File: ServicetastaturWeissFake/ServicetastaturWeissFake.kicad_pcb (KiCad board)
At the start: 2 copper layers, 153.7 x 57.2 mm, 67 parts, among them J1 Automat, SW1 Gewinn, SW10 Lautspr./, SW11 ↓0,10, SW12 ↑0,10, SW13 ↓Serie, SW14 ↑Serie, SW15 Zeit, SW16 ↑1,-, SW17 ↙0,10, SW18 ↙1,-, SW19 Auszahlquote, SW2 Foul, SW20 ↙5,-, SW21 Münzsp., SW22 Sp.Zähl, SW23 Lampen, SW24 Reset, SW25 Initialisieren, SW26 Münzung, SW27 Ende, SW28 ↑0,10, SW29 ↓Serie, SW3 ↙2,-, SW30 ↑Serie, SW31 ↓1,-, SW32 ↑1,-, SW4 HW-Test, SW5 Münzsp., SW6 Sp.Zähl, SW7 Dauerlauf, SW8 Reset, SW9 Initialisieren, U1 CC56-12CGKWA, U2 CC56-12CGKWA, U3 74LS48, U4 74LS145

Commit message: schieberei
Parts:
- added REF**: KiCad-Logo2_6mm_SilkScreen, Symbol:KiCad-Logo2_6mm_SilkScreen, B.Cu at (55.2, 35.6)
- added REF**: Symbol_CC-ShareAlike_CopperTop_Big, Symbol:Symbol_CC-ShareAlike_CopperTop_Big, B.Cu at (88.9, 38.1)
- moved REF** 3.64 mm to (32.4, 36.2)
- moved REF** 2.81 mm to (41.9, 36.8)
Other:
- board text added: "JLCJLCJLCJLC"
- board text added: "Materialwert unter 10€"
- board text added: "Produktionsdaten gibt es gratis online,"
- board text removed: "Wenn du mehr als 15€ bezahlt hast, wurdest du über den Tisch gezogen."

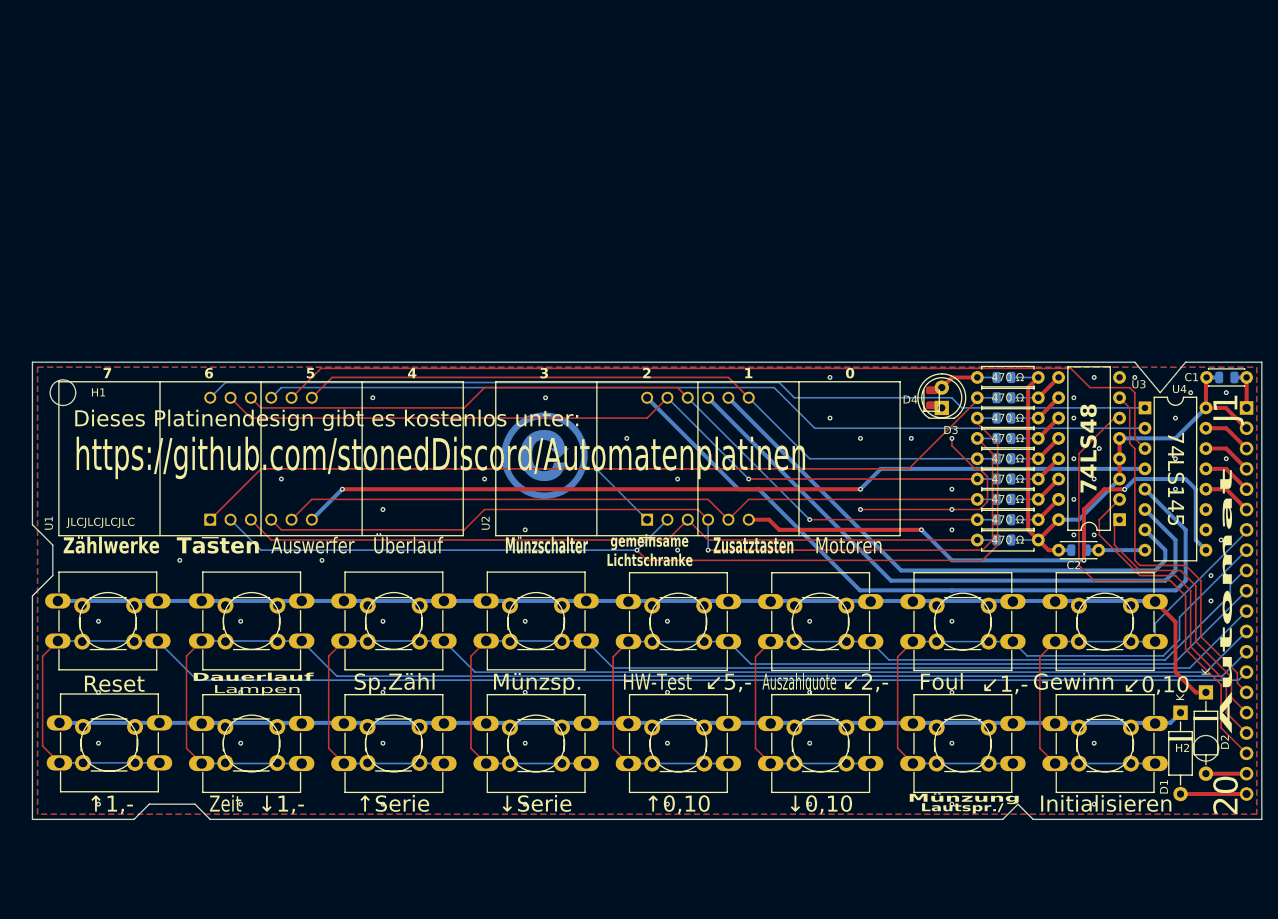
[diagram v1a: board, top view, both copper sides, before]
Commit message: b3f schalter und displays gedreht
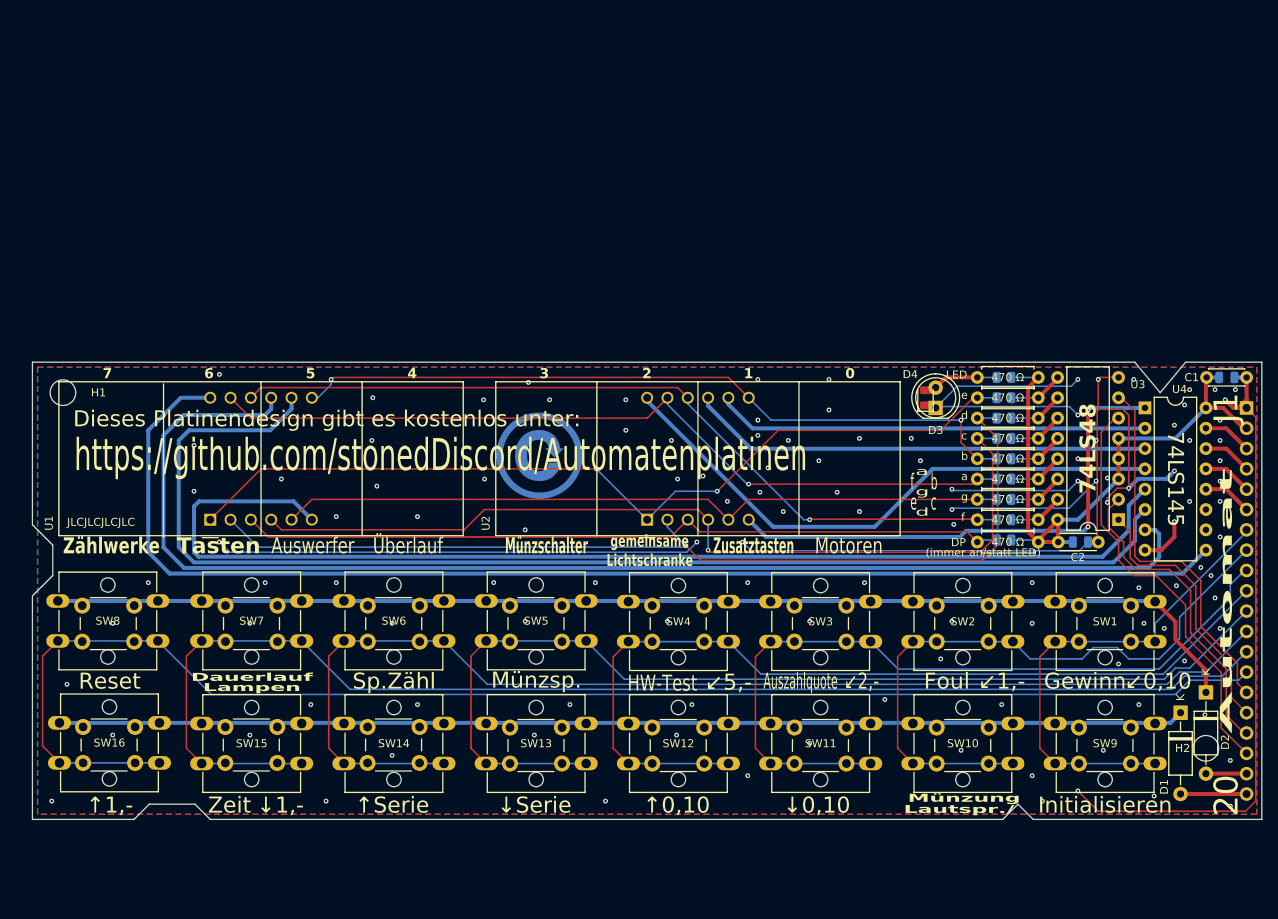
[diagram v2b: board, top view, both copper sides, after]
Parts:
- SW1, SW10, SW11, SW12, SW13, SW14, SW15, SW16, SW2, SW3, SW4, SW5, SW6, SW7, SW8, SW9: footprint Button_Switch_THT:SW_PUSH-12mm -> Button_Switch_THT:SW_SPST_Omron_B3F-40xx
- moved C4 1.03 mm to (155.9, 48.9)
- moved C2 1.02 mm to (153.1, 48.9)
- moved D3 0.76 mm to (137.8, 32.1)
- moved D4 0.76 mm to (136.5, 30.9)
- moved REF** 0.64 mm to (88.3, 38.1)
- moved R8 0.25 mm to (150.6, 48.9)
- moved U3 0.13 mm to (160.7, 46.1)
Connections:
- U4 pad 1: Net-(U1-CC1) -> Net-(U2-CC4)
- U4 pad 2: Net-(U1-CC2) -> Net-(U2-CC3)
- U4 pad 3: Net-(U1-CC3) -> Net-(U2-CC2)
- U4 pad 4: Net-(U1-CC4) -> Net-(U2-CC1)
- U4 pad 5: Net-(U2-CC1) -> Net-(U1-CC4)
- U4 pad 6: Net-(U2-CC2) -> Net-(U1-CC3)
- U4 pad 7: Net-(U2-CC3) -> Net-(U1-CC2)
- U4 pad 9: Net-(U2-CC4) -> Net-(U1-CC1)
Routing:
- net GND: track 39.3 -> 314.2 mm, vias 69 -> 123
- net Net-(U1-CC2): track 111.9 -> 161.2 mm
- net Net-(U1-CC3): track 115.7 -> 156.3 mm
- net Net-(U1-CC1): track 118.9 -> 159.2 mm
- net Net-(U1-CC4): track 106.8 -> 146.1 mm, vias 2 -> 0
- net Net-(U2-CC2): track 77.6 -> 57.9 mm
- net Net-(U2-CC1): track 91.4 -> 72.1 mm
- net Net-(U2-CC3): track 68.9 -> 54.1 mm
- net Net-(U2-CC4): track 74.6 -> 65.7 mm, vias 3 -> 2
- net /A3: track 58.6 -> 52.7 mm
- net Net-(U1-e): track 113.8 -> 109.9 mm, vias 1 -> 2
- net +5V: track 75.1 -> 78.3 mm
- net Net-(U1-b): track 90.9 -> 92.9 mm, vias 0 -> 2
- net /TS7: track 180.4 -> 181.9 mm
- net /TS1: track 78.9 -> 80.3 mm
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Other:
- board text added: "(immer an/statt LED)"
- board text added: "DP"
- board text added: "Die Produkt ionsdaten gibt es gratis online,"
- board text added: "LED"
- board text added: "Spalten"
- board text added: "Wird die Taste {dblquote}HW⁻Test{dblquote} bzw. die Taste {dblquote}Serienspiele{dblquote} betätigt und das Gerät ist mit dieser Sicherung ausgestattet, erscheinen im Testgeräte-Display drei zufällig ausgewählte Ziffern aus dem hexadezimalen Zahlencode."
- board text added: "Zeichen"
- board text added: "a"
- board text added: "b"
- board text added: "c"
- board text added: "d"
- board text added: "e"
- board text added: "f"
- board text added: "g"
- board text removed: "Produktionsdaten gibt es gratis online,"
- board text removed: "Wird die Taste {dblquote}HW⁻Test{dblquote} bzw. die Taste {dblquote}Serienspiele{dblquote} betätigt und das Gerät ist mit dieser Sicherung ausgestattet, erscheinen im Testgeräte-Displaz drei zufällig ausgewählte Ziffern aus dem hexadezimalen Zahlencode."
- board text removed: "ざわ・・・"

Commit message: doppelIC
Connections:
- U3 pad 4: +5V -> Net-(JP1-C)
- U4 pad 10: unconnected-(U4-Q8-Pad10) -> Net-(JP1-A)
- U4 pad 11: unconnected-(U4-Q9-Pad11) -> Net-(JP1-A)
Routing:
- net +5V: track 78.3 -> 103.6 mm
- net GND: vias 123 -> 122
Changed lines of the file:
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@@
 	(net 45 "Net-(U2-CC4)")
 	(net 46 "Net-(U2-CC1)")
-	(net 47 "unconnected-(U4-Q8-Pad10)")
-	(net 48 "unconnected-(U4-Q9-Pad11)")
+	(net 47 "Net-(JP1-C)")
+	(net 48 "Net-(JP1-A)")
 	(footprint "Button_Switch_THT:SW_PUSH_6mm"
 		(layer "F.Cu")
@@
 			(layers "*.Cu" "*.Mask")
 			(remove_unused_layers no)
-			(net 9 "+5V")
+			(net 47 "Net-(JP1-C)")
 			(pinfunction "BI")
 			(pintype "input")
@@
 			(layers "*.Cu" "*.Mask")
 			(remove_unused_layers no)
-			(net 47 "unconnected-(U4-Q8-Pad10)")
+			(net 48 "Net-(JP1-A)")
 			(pinfunction "Q8")
-			(pintype "open_collector+no_connect")
+			(pintype "open_collector")
 		)
 		(pad "11" thru_hole oval
@@
 			(layers "*.Cu" "*.Mask")
 			(remove_unused_layers no)
-			(net 48 "unconnected-(U4-Q9-Pad11)")
+			(net 48 "Net-(JP1-A)")
 			(pinfunction "Q9")
-			(pintype "open_collector+no_connect")
+			(pintype "open_collector")
 		)
 		(pad "12" thru_hole oval
@@
 		(tags "capacitor")
 		(property "Reference" "C4"
-			(at 0 1.68 360)
+			(at 0 1.68 0)
 			(layer "B.SilkS")
 			(effects
@@
 		)
 		(property "Value" "C"
-			(at 0 -1.68 360)
+			(at 0 -1.68 0)
 			(layer "B.Fab")
 			(effects
@@
 		)
 		(fp_text user "${REFERENCE}"
-			(at 0 0 360)
+			(at 0 0 0)
 			(layer "B.Fab")
 			(effects
@@
 	)
 	(segment
-		(start 150.622 48.641)
-		(end 153.035 46.228)
+		(start 150.622 28.321)
+		(end 151.927 27.016)
+		(width 0.2)
+		(layer "F.Cu")
+		(net 9)
+	)
+	(segment
+		(start 159.385 37.211)
+		(end 159.385 39.751)
 		(width 0.5)
 		(layer "F.Cu")
@@
 	)
 	(segment
-		(start 160.655 41.021)
-		(end 160.655 35.941)
+		(start 150.622 48.641)
+		(end 153.035 46.228)
 		(width 0.5)
 		(layer "F.Cu")
@@
 	)
 	(segment
+		(start 165.605173 30.846037)
+		(end 166.118827 30.846037)
+		(width 0.2)
+		(layer "F.Cu")
+		(net 9)
+	)
+	(segment
 		(start 153.115 48.895)
 		(end 150.622 48.895)
@@
 	)
 	(segment
+		(start 159.385 39.751)
+		(end 160.655 41.021)
+		(width 0.5)
+		(layer "F.Cu")
+		(net 9)
+	)
+	(segment
+		(start 166.118827 30.846037)
+		(end 168.643864 28.321)
+		(width 0.2)
+		(layer "F.Cu")
+		(net 9)
+	)
+	(segment
+		(start 160.655 35.941)
+		(end 159.385 37.211)
+		(width 0.5)
+		(layer "F.Cu")
+		(net 9)
+	)
+	(segment
+		(start 168.643864 28.321)
+		(end 171.657 28.321)
+		(width 0.2)
+		(layer "F.Cu")
+		(net 9)
+	)
+	(segment
 		(start 153.035 46.228)
 		(end 153.035 46.101)
@@
 	)
 	(segment
+		(start 151.927 27.016)
+		(end 161.775136 27.016)
+		(width 0.2)
+		(layer "F.Cu")
+		(net 9)
+	)
+	(segment
+		(start 161.775136 27.016)
+		(end 165.605173 30.846037)
+		(width 0.2)
+		(layer "F.Cu")
+		(net 9)
+	)
+	(segment
 		(start 149.352 29.591)
 		(end 149.352 47.625)
@@
 	)
 	(via
-		(at 159.258 40.894)
-		(size 0.6)
-		(drill 0.3)
-		(layers "F.Cu" "B.Cu")
-		(free yes)
-		(net 16)
-	)
-	(via
 		(at 96.52 81.28)
 		(size 0.6)
@@
 	)
 	(via
-		(at 162.56 28.575)
+		(at 162.4963 28.605978)
 		(size 0.6)
 		(drill 0.3)

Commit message: kleine LED
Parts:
- added JP1: Jumper_3_Bridged12, Jumper:SolderJumper-3_P1.3mm_Bridged12_Pad1.0x1.5mm_NumberLabels, B.Cu at (161.0, 31.8)
- added U5: 74LS48, Package_SO:SOIC-16_4.55x10.3mm_P1.27mm, F.Cu at (151.2, 38.1)
- added U6: 74LS145, Package_SO:SOIC-16_4.55x10.3mm_P1.27mm, F.Cu at (165.2, 41.3)
- C3, C4, R10, R11, R12, R13, R14, R15, R16, R17, R18: moved to F.Cu
- D3: footprint LED_THT:LED_D5.0mm -> LED_THT:LED_D3.0mm
- moved C4 9.34 mm to (146.6, 48.5), turned to 180 degrees
- moved C2 6.53 mm to (150.1, 54.7), turned to -90 degrees
- moved R6 5.57 mm to (145.7, 43.6)
- moved R7 5.35 mm to (145.7, 41.5)
- moved R1 5.18 mm to (145.7, 39.5)
- moved R15 5.12 mm to (141.9, 43.6)
- moved R2 5.06 mm to (145.7, 37.5)
- moved R3 4.98 mm to (145.7, 35.4)
- moved R4 4.95 mm to (145.7, 33.4)
- moved R16 4.89 mm to (141.9, 41.5)
- moved R10 4.70 mm to (141.9, 39.5)
- moved R11 4.56 mm to (141.9, 37.5)
- moved R12 4.47 mm to (141.9, 35.4)
- moved R13 4.44 mm to (141.9, 33.4)
- moved R8 3.68 mm to (148.1, 46.2)
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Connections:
- R17 pad 2: Net-(U1-DPX) -> unconnected-(R17-Pad2)
- R8 pad 2: Net-(U1-DPX) -> unconnected-(R17-Pad2)
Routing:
- net GND: track 314.2 -> 111.9 mm, vias 122 -> 85
- net Net-(U1-DPX): track 96.3 -> 56.4 mm
- net Net-(JP1-A): track 0.00 -> 30.7 mm, vias 0 -> 1
- net Net-(U2-CC3): track 54.1 -> 79.2 mm
- net Net-(U2-CC2): track 57.9 -> 78.7 mm
- net Net-(U1-d): track 122.5 -> 103.6 mm
- net Net-(U1-c): track 112.7 -> 95.1 mm, vias 1 -> 2
- net Net-(JP1-C): track 0.00 -> 11.8 mm
- net /A1: track 33.5 -> 42.8 mm, vias 0 -> 2
- net /A3: track 52.7 -> 61.9 mm
- net Net-(U2-CC1): track 72.1 -> 80.7 mm
- net /A0: track 46.7 -> 54.9 mm
- net Net-(U1-e): track 109.9 -> 117.5 mm, vias 2 -> 1
- net Net-(U1-b): track 92.9 -> 86.4 mm, vias 2 -> 1
- net Net-(U1-CC1): track 159.2 -> 165.7 mm
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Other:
- outline, holes or cut-outs redrawn
- board text removed: "(immer an/statt LED)"
- board text removed: "DP"
- board text removed: "LED"
- board text removed: "Spalten"
- board text removed: "Zeichen"
- board text removed: "a"
- board text removed: "b"
- board text removed: "c"
- board text removed: "d"
- board text removed: "e"
- board text removed: "f"
- board text removed: "g"

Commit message: rumgeschiebe
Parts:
- moved SW8 0.20 mm to (28.3, 56.3)
- moved SW16 0.08 mm to (28.3, 71.6)

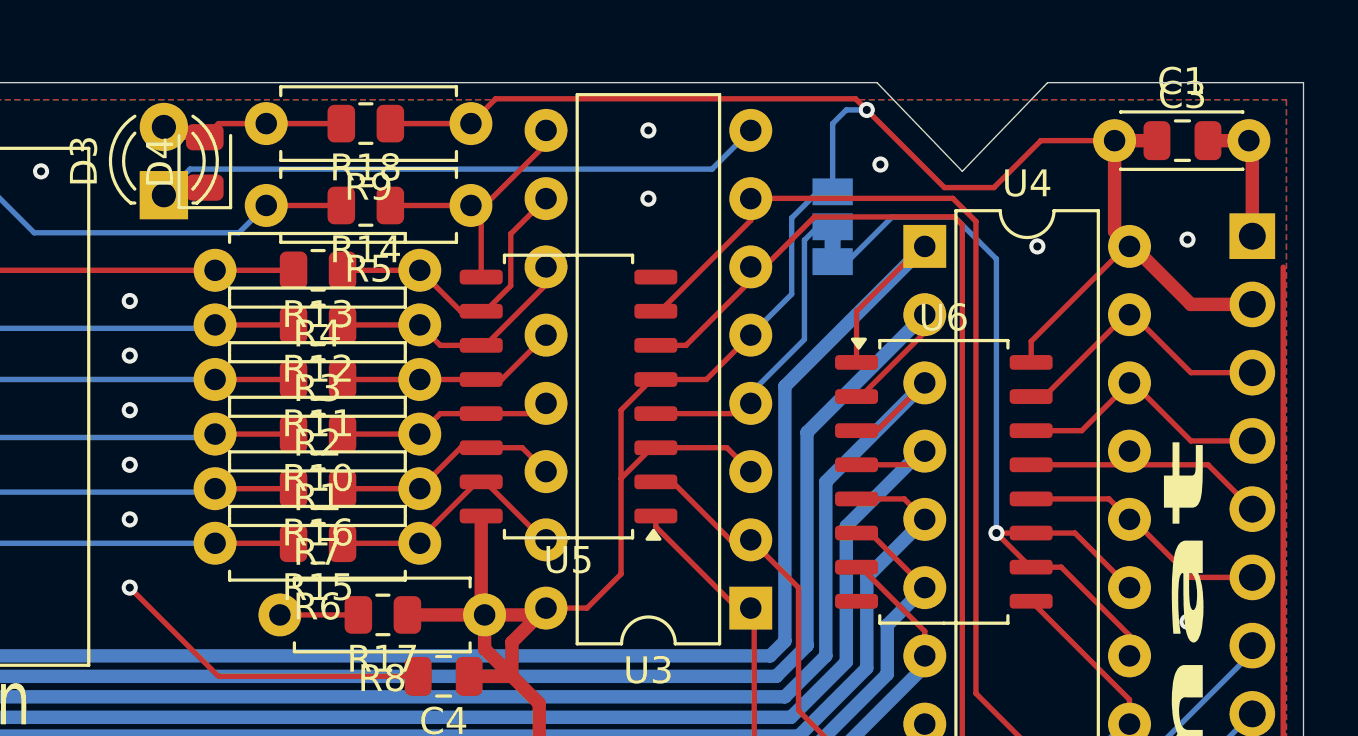
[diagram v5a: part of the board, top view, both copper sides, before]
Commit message: Update ServicetastaturWeissFake.kicad_pcb
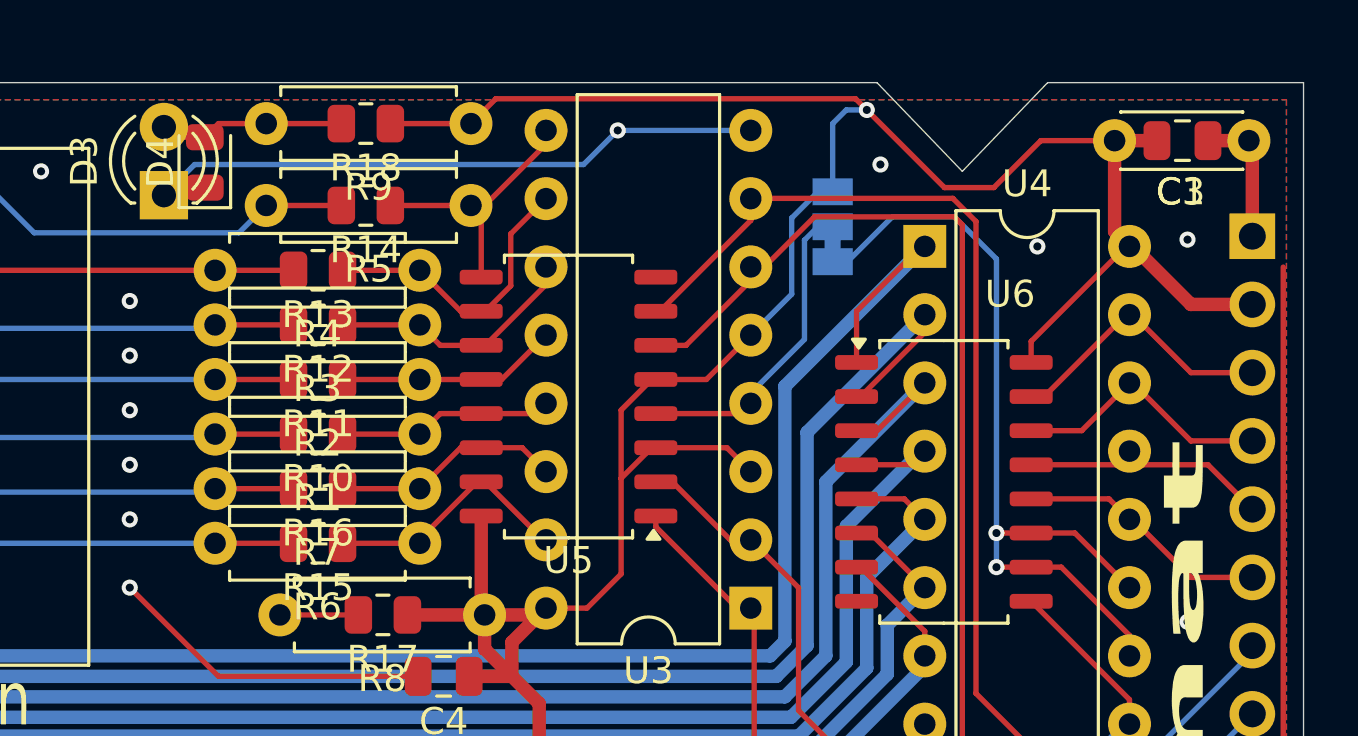
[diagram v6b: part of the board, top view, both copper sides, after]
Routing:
- net Net-(JP1-A): track 30.7 -> 31.5 mm, vias 1 -> 2
- net GND: vias 85 -> 84
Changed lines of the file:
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@@
 		(tags "SOIC SO")
 		(property "Reference" "U6"
-			(at 0 -6.1 0)
+			(at 2.465 -6.985 0)
 			(layer "F.SilkS")
 			(effects
@@
 		(tags "capacitor")
 		(property "Reference" "C3"
-			(at 0 -1.68 0)
+			(at -0.066 1.905 0)
 			(layer "F.SilkS")
 			(effects
@@
 		(tags "C Disc series Radial pin pitch 5.00mm  diameter 4.3mm width 1.9mm Capacitor")
 		(property "Reference" "C1"
-			(at 2.5 -2.2 0)
+			(at 2.46 1.905 0)
 			(layer "F.SilkS")
 			(effects
@@
 	)
 	(via
-		(at 154.178 30.734)
+		(at 153.035 28.194)
 		(size 0.6)
 		(drill 0.3)
@@
 	)
 	(via
-		(at 154.178 28.194)
-		(size 0.6)
-		(drill 0.3)
-		(layers "F.Cu" "B.Cu")
-		(free yes)
-		(net 16)
-	)
-	(via
 		(at 34.925 73.025)
 		(size 0.6)
@@
 	)
 	(segment
-		(start 157.988 28.194)
-		(end 156.548 29.634)
+		(start 153.035 28.194)
+		(end 151.765 29.464)
+		(width 0.2)
+		(layer "B.Cu")
+		(net 16)
+	)
+	(segment
+		(start 151.765 29.464)
+		(end 137.287 29.464)
 		(width 0.2)
 		(layer "B.Cu")
@@
 	)
 	(segment
-		(start 156.548 29.634)
-		(end 137.117 29.634)
+		(start 157.988 28.194)
+		(end 153.035 28.194)
 		(width 0.2)
 		(layer "B.Cu")
@@
 	)
 	(segment
-		(start 137.117 29.634)
+		(start 137.287 29.464)
 		(end 136.144 30.607)
 		(width 0.2)
@@
 	)
 	(segment
-		(start 168.402008 44.45)
-		(end 167.132004 43.179996)
+		(start 168.425 44.45)
+		(end 167.132 44.45)
 		(width 0.2)
 		(layer "F.Cu")
@@
 	)
 	(segment
-		(start 168.425 44.45)
-		(end 168.402008 44.45)
-		(width 0.2)
-		(layer "F.Cu")
-		(net 48)
-	)
-	(segment
 		(start 168.425 43.18)
 		(end 167.132008 43.18)
@@
 	)
 	(via
+		(at 167.132 44.45)
+		(size 0.6)
+		(drill 0.3)
+		(layers "F.Cu" "B.Cu")
+		(net 48)
+	)
+	(via
 		(at 167.132004 43.179996)
 		(size 0.6)
@@
 		(width 0.2)
 		(layer "B.Cu")
+		(net 48)
+	)
+	(segment
+		(start 167.132 43.18)
+		(end 167.132004 43.179996)
+		(width 0.2)
+		(layer "B.Cu")
+		(net 48)
+	)
+	(segment
+		(start 167.132 44.45)
+		(end 167.132 43.18)
+		(width 0.2)
+		(layer "B.Cu")
